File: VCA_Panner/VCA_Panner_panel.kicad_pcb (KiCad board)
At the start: 2 copper layers, 50.8 x 128.5 mm, 0 parts

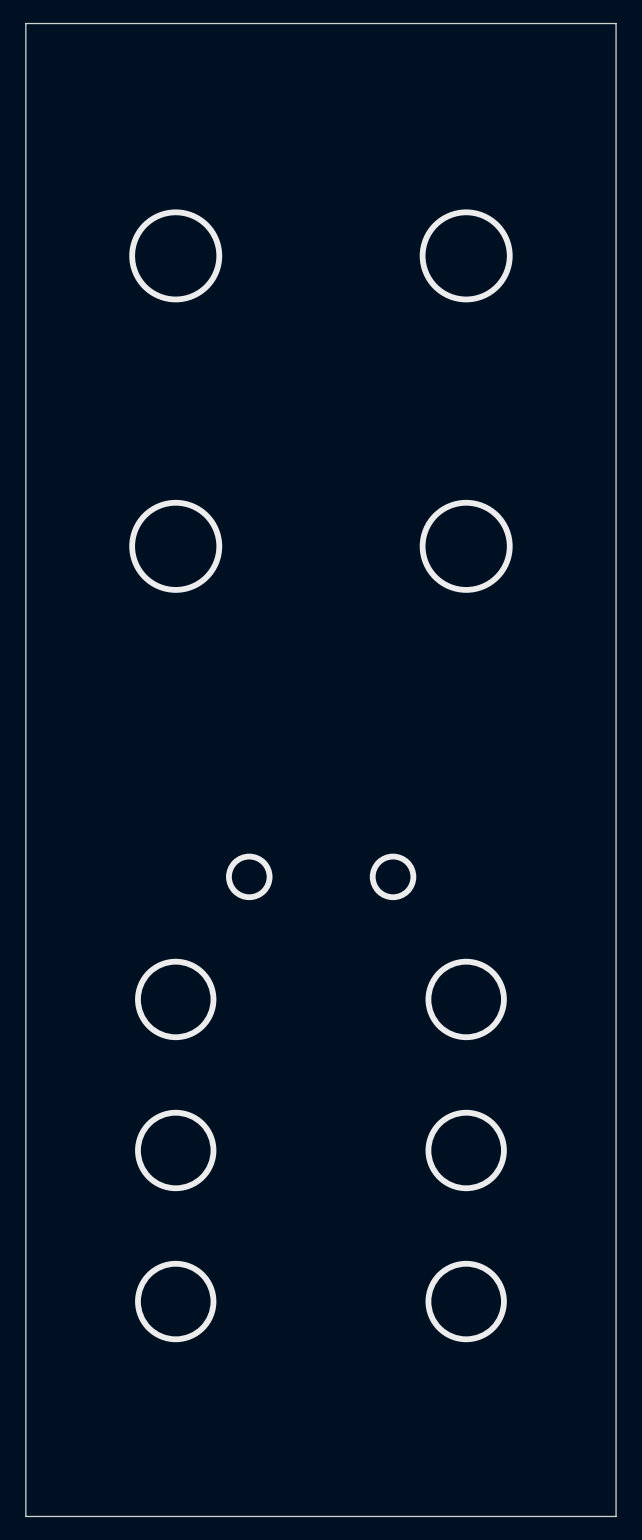
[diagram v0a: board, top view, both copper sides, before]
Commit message: vca panner
All done, first set ordered
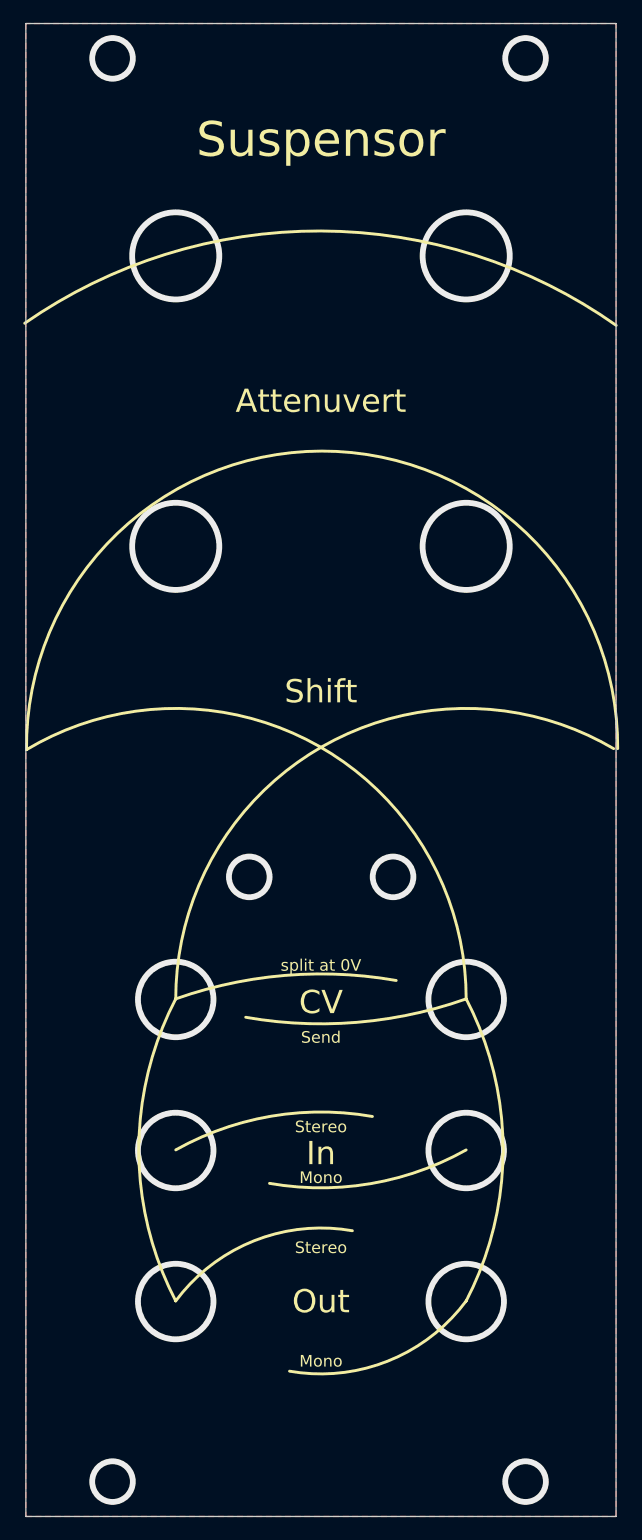
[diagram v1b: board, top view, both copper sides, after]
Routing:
- net GND: vias 12 -> 16
- added copper zone on F.Cu, net GND
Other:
- board text added: "Attenuvert"
- board text added: "CV"
- board text added: "In"
- board text added: "Mono"
- board text added: "Out"
- board text added: "Send"
- board text added: "Shift"
- board text added: "Stereo"
- board text added: "Suspensor"
- board text added: "split at 0V"
